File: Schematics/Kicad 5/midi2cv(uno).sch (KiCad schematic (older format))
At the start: 20 parts, among them IC1 LM324N, J1 Arduino_Uno_Headers, J3 CONN_025MM, J4 MIDI-DIN

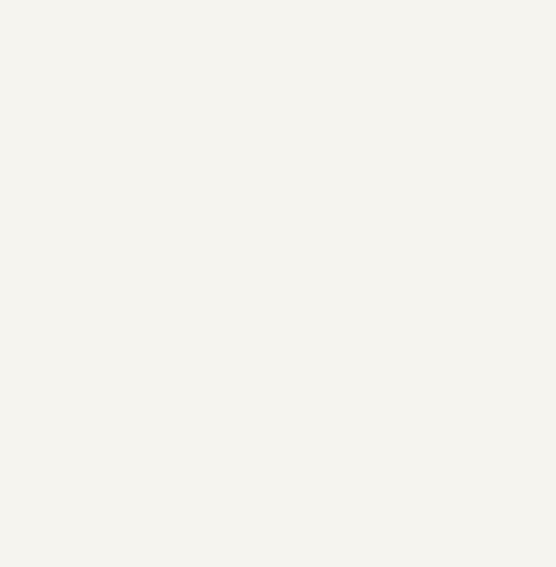
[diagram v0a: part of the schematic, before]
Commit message: addded Arduino_Uno_Header symbol
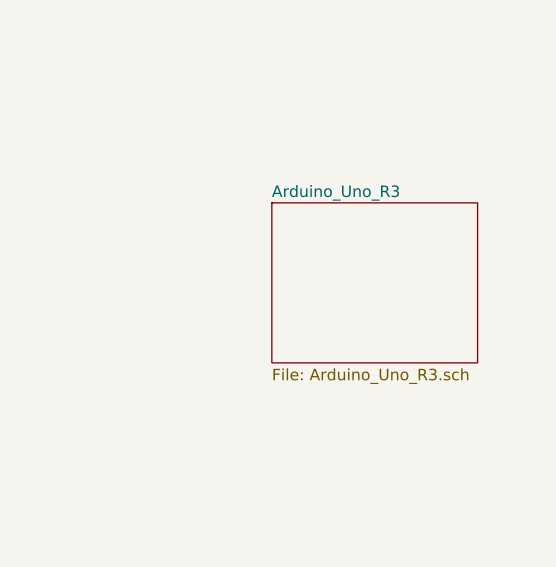
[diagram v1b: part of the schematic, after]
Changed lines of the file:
@@
 $Descr User 9449 7874
 encoding utf-8
-Sheet 1 1
+Sheet 1 2
 Title "MIDI2CV"
 Date "2018-08-07"
@@
 	1800 4250 1800 3850
 Connection ~ 1800 3850
+$Sheet
+S 10250 2400 900  700
+U 5B6B1999
+F0 "Arduino_Uno_R3" 50
+F1 "Arduino_Uno_R3.sch" 50
+$EndSheet
 $EndSCHEMATC
